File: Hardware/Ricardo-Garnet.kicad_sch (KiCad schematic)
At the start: 46 parts, among them J1 RBUS, P4 IN+, P5 IN-, P6 MOTOR1, P7 MOTOR2, P9 MOTOR3, U1 ESP32-S3, Y2 R940000171

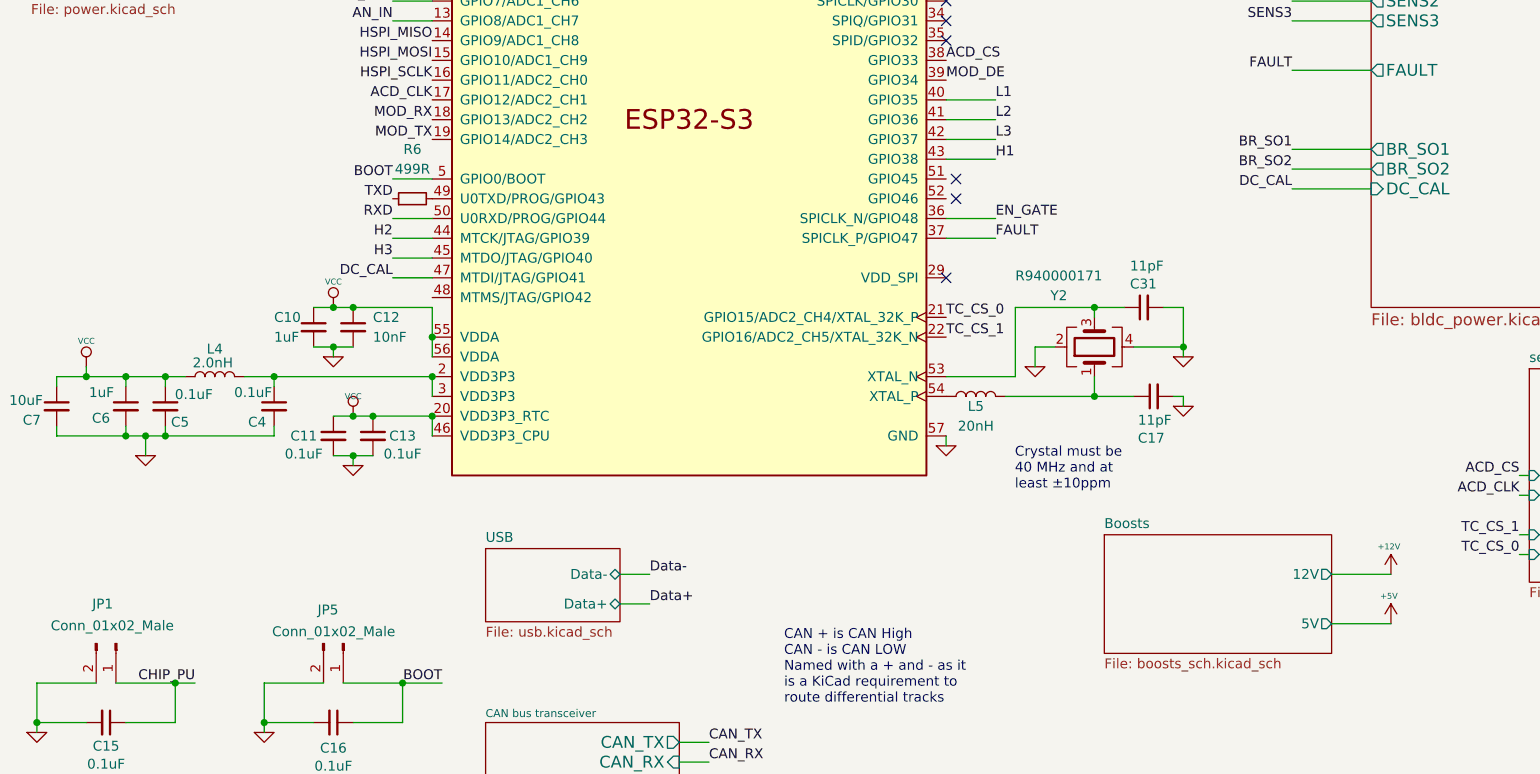
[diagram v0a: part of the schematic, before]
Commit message: removed voltage pt sensing capabilities
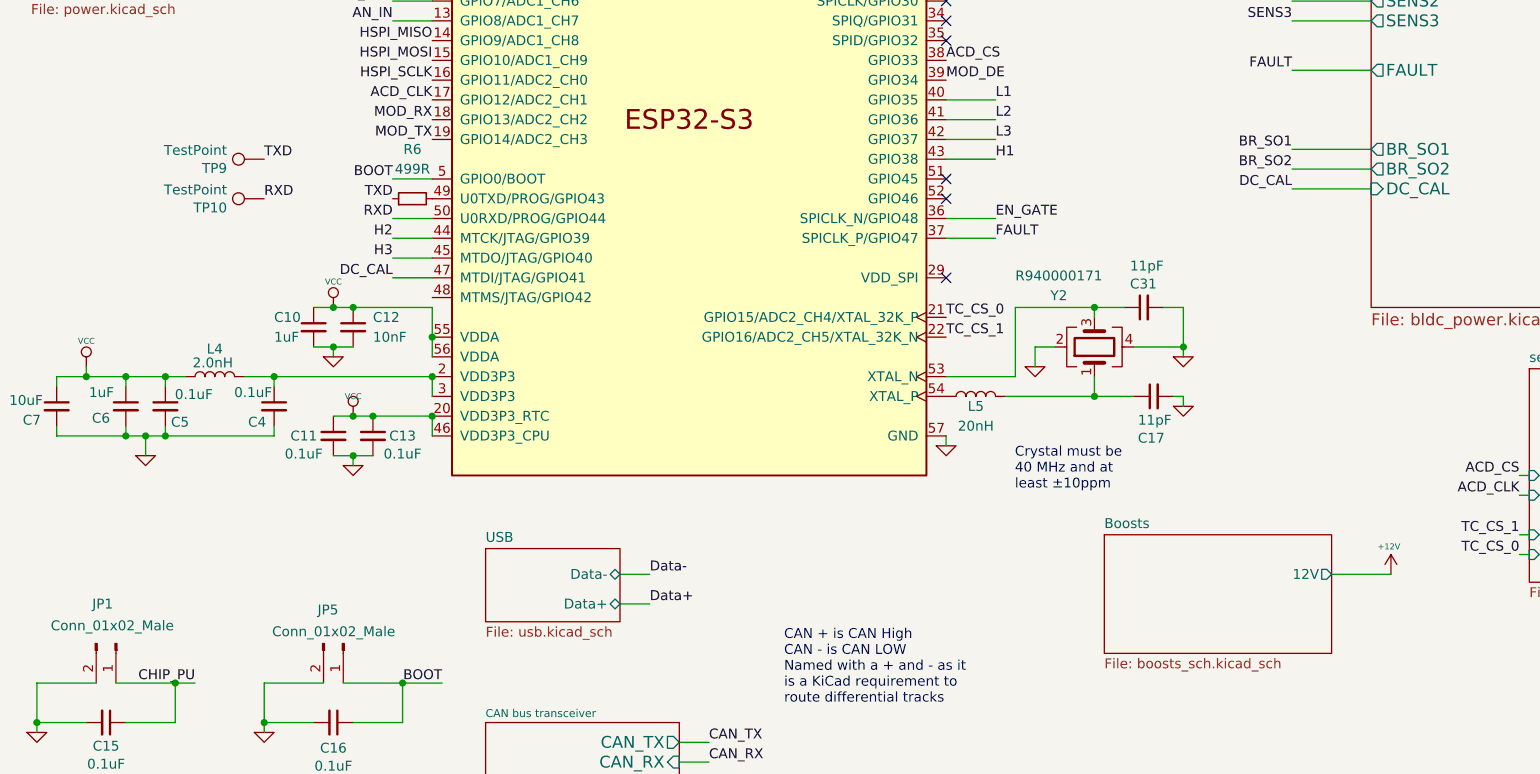
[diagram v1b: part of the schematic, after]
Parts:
- added TP10, TP9: TestPoint, TestPoint:TestPoint_Pad_D1.0mm, symbol Connector:TestPoint
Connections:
- net RXD: now also TP10.1
- net TXD: now also TP9.1
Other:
- sheet Boosts ports: added none; removed 5V
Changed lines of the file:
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@@
 	)
 	(no_connect
-		(at 134.62 104.14)
+		(at 133.35 104.14)
 	)
 	(no_connect
-		(at 134.62 101.6)
+		(at 133.35 101.6)
 	)
 	(no_connect
@@
 	(wire
 		(pts
-			(xy 182.88 158.75) (xy 190.5 158.75)
-		)
-		(stroke
-			(width 0)
-			(type default)
-		)
-	)
-	(wire
-		(pts
 			(xy 220.98 26.67) (xy 220.98 29.21)
 		)
@@
 		)
 	)
+	(label "RXD"
+		(at 45.72 104.14 0)
+		(effects
+			(font
+				(size 1.27 1.27)
+			)
+			(justify left bottom)
+		)
+	)
 	(label "CAN-"
 		(at 102.87 182.88 0)
@@
 		)
 	)
+	(label "TXD"
+		(at 45.72 99.06 0)
+		(effects
+			(font
+				(size 1.27 1.27)
+			)
+			(justify left bottom)
+		)
+	)
 	(label "AN_IN"
 		(at 238.76 21.59 0)
@@
 	)
 	(symbol
+		(lib_id "Connector:TestPoint")
+		(at 45.72 99.06 90)
+		(unit 1)
+		(exclude_from_sim no)
+		(in_bom yes)
+		(on_board yes)
+		(dnp no)
+		(property "Reference" "TP9"
+			(at 40.9448 100.2284 90)
+			(effects
+				(font
+					(size 1.27 1.27)
+				)
+				(justify left)
+			)
+		)
+		(property "Value" "TestPoint"
+			(at 40.9448 97.917 90)
+			(effects
+				(font
+					(size 1.27 1.27)
+				)
+				(justify left)
+			)
+		)
+		(property "Footprint" "TestPoint:TestPoint_Pad_D1.0mm"
+			(at 45.72 93.98 0)
+			(effects
+				(font
+					(size 1.27 1.27)
+				)
+				(hide yes)
+			)
+		)
+		(property "Datasheet" "~"
+			(at 45.72 93.98 0)
+			(effects
+				(font
+					(size 1.27 1.27)
+				)
+				(hide yes)
+			)
+		)
+		(property "Description" ""
+			(at 45.72 99.06 0)
+			(effects
+				(font
+					(size 1.27 1.27)
+				)
+				(hide yes)
+			)
+		)
+		(pin "1"
+		)
+		(instances
+			(project "Ricardo-Garnet"
+				(path "/a4c716a5-e5f4-4cd7-812e-2c21e63f692f"
+					(reference "TP9")
+					(unit 1)
+				)
+			)
+		)
+	)
+	(symbol
 		(lib_id "Device:LED_Small")
 		(at 25.4 38.1 0)
@@
 	)
 	(symbol
-		(lib_name "+5V_9")
-		(lib_id "BLDC_4-rescue:+5V")
-		(at 190.5 158.75 0)
-		(unit 1)
-		(exclude_from_sim no)
-		(in_bom yes)
-		(on_board yes)
-		(dnp no)
-		(property "Reference" "#PWR065"
-			(at 190.5 156.464 0)
-			(effects
-				(font
-					(size 0.508 0.508)
-				)
-				(hide yes)
-			)
-		)
-		(property "Value" "+5V"
-			(at 190.246 155.194 0)
-			(effects
-				(font
-					(size 0.762 0.762)
-				)
-			)
-		)
-		(property "Footprint" ""
-			(at 190.5 158.75 0)
-			(effects
-				(font
-					(size 1.524 1.524)
-				)
-				(hide yes)
-			)
-		)
-		(property "Datasheet" ""
-			(at 190.5 158.75 0)
-			(effects
-				(font
-					(size 1.524 1.524)
-				)
-				(hide yes)
-			)
-		)
-		(property "Description" ""
-			(at 190.5 158.75 0)
-			(effects
-				(font
-					(size 1.27 1.27)
-				)
-			)
-		)
-		(pin "1"
-		)
-		(instances
-			(project "BLDC_4"
-				(path "/a4c716a5-e5f4-4cd7-812e-2c21e63f692f"
-					(reference "#PWR065")
-					(unit 1)
-				)
-			)
-		)
-	)
-	(symbol
 		(lib_name "GND-RESCUE-BLDC_4_20")
 		(lib_id "BLDC_4-rescue:GND-RESCUE-BLDC_4")
@@
 	)
 	(symbol
+		(lib_id "Connector:TestPoint")
+		(at 45.72 104.14 90)
+		(unit 1)
+		(exclude_from_sim no)
+		(in_bom yes)
+		(on_board yes)
+		(dnp no)
+		(property "Reference" "TP10"
+			(at 40.9448 105.3084 90)
+			(effects
+				(font
+					(size 1.27 1.27)
+				)
+				(justify left)
+			)
+		)
+		(property "Value" "TestPoint"
+			(at 40.9448 102.997 90)
+			(effects
+				(font
+					(size 1.27 1.27)
+				)
+				(justify left)
+			)
+		)
+		(property "Footprint" "TestPoint:TestPoint_Pad_D1.0mm"
+			(at 45.72 99.06 0)
+			(effects
+				(font
+					(size 1.27 1.27)
+				)
+				(hide yes)
+			)
+		)
+		(property "Datasheet" "~"
+			(at 45.72 99.06 0)
+			(effects
+				(font
+					(size 1.27 1.27)
+				)
+				(hide yes)
+			)
+		)
+		(property "Description" ""
+			(at 45.72 104.14 0)
+			(effects
+				(font
+					(size 1.27 1.27)
+				)
+				(hide yes)
+			)
+		)
+		(pin "1"
+		)
+		(instances
+			(project "Ricardo-Garnet"
+				(path "/a4c716a5-e5f4-4cd7-812e-2c21e63f692f"
+					(reference "TP10")
+					(unit 1)
+				)
+			)
+		)
+	)
+	(symbol
 		(lib_id "Device:C_Small")
 		(at 46.99 130.81 0)
@@
 		)
 		(instances
-			(project "BLDC_4"
+			(project "Ricardo-Garnet"
 				(path "/a4c716a5-e5f4-4cd7-812e-2c21e63f692f"
 					(page "6")
@@
 		)
 		(instances
-			(project "BLDC_4"
+			(project "Ricardo-Garnet"
 				(path "/a4c716a5-e5f4-4cd7-812e-2c21e63f692f"
 					(page "7")
@@
 		)
 		(instances
-			(project "BLDC_4"
+			(project "Ricardo-Garnet"
 				(path "/a4c716a5-e5f4-4cd7-812e-2c21e63f692f"
 					(page "2")
@@
 		)
 		(instances
-			(project "BLDC_4"
+			(project "Ricardo-Garnet"
 				(path "/a4c716a5-e5f4-4cd7-812e-2c21e63f692f"
 					(page "5")
@@
 		)
 		(instances
-			(project "BLDC_4"
+			(project "Ricardo-Garnet"
 				(path "/a4c716a5-e5f4-4cd7-812e-2c21e63f692f"
 					(page "3")
@@
 			)
 		)
-		(pin "5V" output
-			(at 182.88 158.75 0)
-			(effects
-				(font
-					(size 1.27 1.27)
-				)
-				(justify right)
-			)
-		)
 		(instances
-			(project "BLDC_4"
+			(project "Ricardo-Garnet"
 				(path "/a4c716a5-e5f4-4cd7-812e-2c21e63f692f"
 					(page "4")
@@
 		)
 		(instances
-			(project "BLDC_4"
+			(project "Ricardo-Garnet"
 				(path "/a4c716a5-e5f4-4cd7-812e-2c21e63f692f"
 					(page "8")

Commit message: chatting to fang
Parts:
- C2, C41: footprint CRF1:SMD-0603_c -> Capacitor_SMD:C_0603_1608Metric
- R1, R3: footprint CRF1:SMD-0603_r -> Resistor_SMD:R_0603_1608Metric
- R2, R4: footprint CRF1:SMD-0603_r -> Resistor_SMD:R_0402_1005Metric
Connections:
- net ACD_CS: now also U1.36 (SPICLK_N/GPIO48); no longer U1.38 (GPIO33)
- net AN_IN: now also U1.12 (GPIO7/ADC1_CH6); no longer U1.13 (GPIO8/ADC1_CH7)
- net BR_SO2: now also U1.10 (GPIO5/ADC1_CH4); no longer U1.12 (GPIO7/ADC1_CH6)
- net EN_GATE: now also U1.39 (GPIO34); no longer U1.36 (SPICLK_N/GPIO48)
- net FAULT: now also U1.48 (MTMS/JTAG/GPIO42); no longer U1.37 (SPICLK_P/GPIO47)
- net H1: now also U1.45 (MTDO/JTAG/GPIO40); no longer U1.43 (GPIO38)
- net H2: now also U1.43 (GPIO38); no longer U1.44 (MTCK/JTAG/GPIO39)
- net H3: now also U1.41 (GPIO36); no longer U1.45 (MTDO/JTAG/GPIO40)
- net L1: now also U1.44 (MTCK/JTAG/GPIO39); no longer U1.40 (GPIO35)
- net L2: now also U1.42 (GPIO37); no longer U1.41 (GPIO36)
- net L3: now also U1.40 (GPIO35); no longer U1.42 (GPIO37)
- net MOD_DE: now also U1.27 (GPIO21); no longer U1.39 (GPIO34)
- net MOS_TEMP: now also U1.13 (GPIO8/ADC1_CH7); no longer U1.10 (GPIO5/ADC1_CH4)
- net SENS1: now also U1.7 (GPIO2/ADC1_CH1); no longer U1.6 (GPIO1/ADC1_CH0)
- net SENS2: now also U1.9 (GPIO4/ADC1_CH3); no longer U1.7 (GPIO2/ADC1_CH1)
- net SENS3: now also U1.6 (GPIO1/ADC1_CH0); no longer U1.9 (GPIO4/ADC1_CH3)
- no-connect marks 12 -> 15

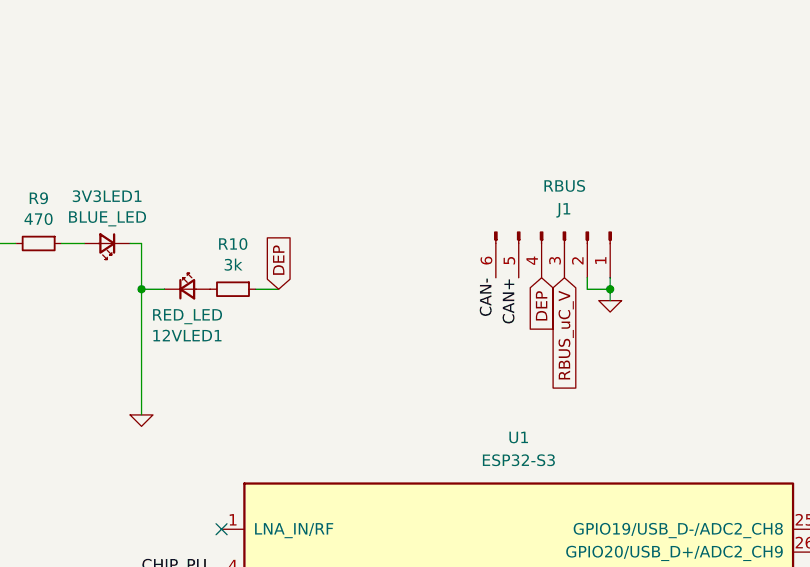
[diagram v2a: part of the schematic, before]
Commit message: updated settled pcb design
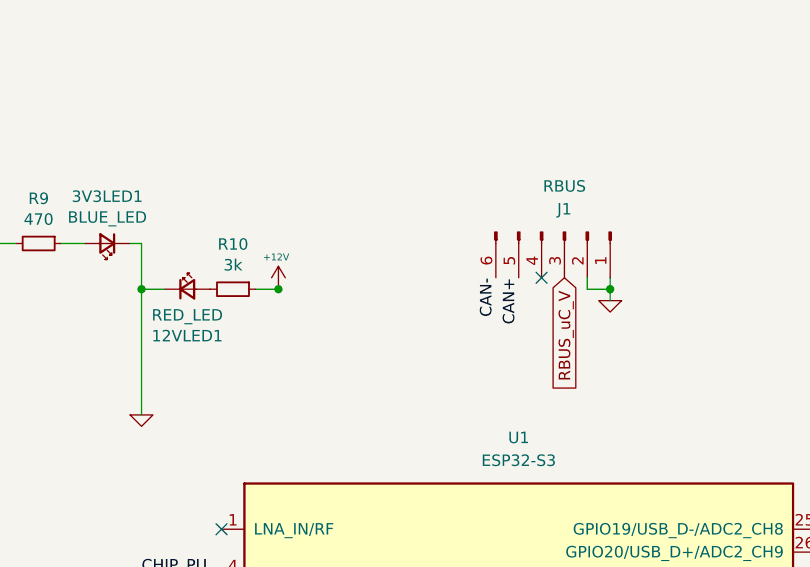
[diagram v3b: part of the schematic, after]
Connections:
- net +12V: now also R10.1
- net DEP: no longer names the net of J1.4 (Pin_4)
- net DEP: no longer R10.1
- no-connect marks 15 -> 16
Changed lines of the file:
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@@
 	)
 	(junction
+		(at 73.6308 26.67)
+		(diameter 0)
+		(color 0 0 0 0)
+	)
+	(junction
 		(at 33.02 127)
 		(diameter 0)
@@
 	)
 	(no_connect
+		(at 102.87 25.4)
+	)
+	(no_connect
 		(at 133.35 109.22)
 	)
@@
 	(wire
 		(pts
-			(xy 73.66 26.67) (xy 71.12 26.67)
+			(xy 73.66 26.67) (xy 73.6308 26.67)
 		)
 		(stroke
@@
 	(wire
 		(pts
+			(xy 73.6308 26.67) (xy 71.12 26.67)
+		)
+		(stroke
+			(width 0)
+			(type default)
+		)
+	)
+	(wire
+		(pts
 			(xy 30.48 184.15) (xy 30.48 186.69)
 		)
@@
 		)
 	)
-	(global_label "DEP"
-		(shape input)
-		(at 73.66 26.67 90)
-		(fields_autoplaced yes)
-		(effects
-			(font
-				(size 1.27 1.27)
-			)
-			(justify left)
-		)
-		(property "Intersheetrefs" "${INTERSHEET_REFS}"
-			(at 73.66 20.65 90)
-			(effects
-				(font
-					(size 1.27 1.27)
-				)
-				(justify left)
-				(hide yes)
-			)
-		)
-	)
-	(global_label "DEP"
-		(shape input)
-		(at 102.87 25.4 270)
-		(fields_autoplaced yes)
-		(effects
-			(font
-				(size 1.27 1.27)
-			)
-			(justify right)
-		)
-		(property "Intersheetrefs" "${INTERSHEET_REFS}"
-			(at 102.87 31.42 90)
-			(effects
-				(font
-					(size 1.27 1.27)
-				)
-				(justify right)
-				(hide yes)
-			)
-		)
-	)
 	(global_label "V_SUPPLY"
 		(shape input)
@@
 					(unit 1)
 				)
+			)
+		)
+	)
+	(symbol
+		(lib_name "+5V_9")
+		(lib_id "BLDC_4-rescue:+5V")
+		(at 73.6308 26.67 0)
+		(unit 1)
+		(exclude_from_sim no)
+		(in_bom yes)
+		(on_board yes)
+		(dnp no)
+		(property "Reference" "#PWR052"
+			(at 73.6308 24.384 0)
+			(effects
+				(font
+					(size 0.508 0.508)
+				)
+				(hide yes)
+			)
+		)
+		(property "Value" "+12V"
+			(at 73.3768 23.114 0)
+			(effects
+				(font
+					(size 0.762 0.762)
+				)
+			)
+		)
+		(property "Footprint" ""
+			(at 73.6308 26.67 0)
+			(effects
+				(font
+					(size 1.524 1.524)
+				)
+				(hide yes)
+			)
+		)
+		(property "Datasheet" ""
+			(at 73.6308 26.67 0)
+			(effects
+				(font
+					(size 1.524 1.524)
+				)
+				(hide yes)
+			)
+		)
+		(property "Description" ""
+			(at 73.6308 26.67 0)
+			(effects
+				(font
+					(size 1.27 1.27)
+				)
+			)
+		)
+		(pin "1"
+		)
+		(instances
+			(project "Ricardo-Garnet"
+				(path "/a4c716a5-e5f4-4cd7-812e-2c21e63f692f"
+					(reference "#PWR052")
+					(unit 1)
+				)

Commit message: close to 1st done
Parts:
- removed P6: MOTOR1, CRF1:1PAD_4x5mm, symbol BLDC_4-rescue:CONN_1
- removed P7: MOTOR2, CRF1:1PAD_4x5mm, symbol BLDC_4-rescue:CONN_1
- removed P9: MOTOR3, CRF1:1PAD_4x5mm, symbol BLDC_4-rescue:CONN_1
- removed R53, R54: SHUNT, CRF1:WSLP2726, symbol crf_1:SHUNT
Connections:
- net ACD_CLK: now also U1.12 (GPIO7/ADC1_CH6); no longer U1.17 (GPIO12/ADC2_CH1)
- net ACD_CS: now also U1.21 (GPIO15/ADC2_CH4/XTAL_32K_P); no longer U1.36 (SPICLK_N/GPIO48)
- net AN_IN: now also U1.18 (GPIO13/ADC2_CH2); no longer U1.12 (GPIO7/ADC1_CH6)
- net BR_SO1: now also U1.6 (GPIO1/ADC1_CH0); no longer U1.11 (GPIO6/ADC1_CH5)
- net BR_SO2: now also U1.7 (GPIO2/ADC1_CH1); no longer U1.10 (GPIO5/ADC1_CH4)
- net HSPI_MISO: now also U1.15 (GPIO10/ADC1_CH9); no longer U1.14 (GPIO9/ADC1_CH8)
- net HSPI_MOSI: now also U1.16 (GPIO11/ADC2_CH0); no longer U1.15 (GPIO10/ADC1_CH9)
- net HSPI_SCLK: now also U1.17 (GPIO12/ADC2_CH1); no longer U1.16 (GPIO11/ADC2_CH0)
- net MOD_DE: now also U1.36 (SPICLK_N/GPIO48); no longer U1.27 (GPIO21)
- net MOD_RX: now also U1.14 (GPIO9/ADC1_CH8); no longer U1.18 (GPIO13/ADC2_CH2)
- net MOD_TX: now also U1.13 (GPIO8/ADC1_CH7); no longer U1.19 (GPIO14/ADC2_CH3)
- net MOS_TEMP: now also U1.19 (GPIO14/ADC2_CH3); no longer U1.13 (GPIO8/ADC1_CH7)
- net SENS1: now also U1.10 (GPIO5/ADC1_CH4); no longer U1.7 (GPIO2/ADC1_CH1)
- net SENS2: now also U1.11 (GPIO6/ADC1_CH5); no longer U1.9 (GPIO4/ADC1_CH3)
- net SENS3: now also U1.9 (GPIO4/ADC1_CH3); no longer U1.6 (GPIO1/ADC1_CH0)
- net TC_CS_0: now also U1.22 (GPIO16/ADC2_CH5/XTAL_32K_N); no longer U1.21 (GPIO15/ADC2_CH4/XTAL_32K_P)
- net TC_CS_1: now also U1.27 (GPIO21); no longer U1.22 (GPIO16/ADC2_CH5/XTAL_32K_N)
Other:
- sheet Mosfet driver ports: added GH_A, GH_B, GH_C, GL_A, GL_B, GL_C, SH_A, SH_B, SH_C, SL_A, SL_B, SL_C, SN1, SN2, SP1, SP2; removed H1_LOW, H1_VS, H2_LOW, H2_VS, H3_LOW, H3_VS, M_H1, M_H2, M_H3, M_L1, M_L2, M_L3, SH1_A, SH1_B, SH2_A, SH2_B
- sheet Power MOSFETS ports: added GH_A, GH_B, GH_C, GL_A, GL_B, GL_C, SH_A, SH_B, SH_C, SL_A, SL_B, SL_C, SN1, SN2, SP1, SP2; removed H1_LOW, H1_VS, H2_LOW, H2_VS, H3_LOW, H3_VS, M_H1, M_H2, M_H3, M_L1, M_L2, M_L3, PHASE_1, PHASE_2, PHASE_3

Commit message: final touches and adding encoder
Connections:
- net ENCODER_CS: now reaches U1.37 (SPICLK_P/GPIO47)
- no-connect marks 16 -> 15
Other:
- sheet sensors ports: added ENCODER_CS; removed none
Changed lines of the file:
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@@
 	)
 	(no_connect
-		(at 133.35 109.22)
-	)
-	(no_connect
 		(at 133.35 86.36)
 	)
@@
 	(wire
 		(pts
+			(xy 133.35 109.22) (xy 139.7 109.22)
+		)
+		(stroke
+			(width 0)
+			(type default)
+		)
+	)
+	(wire
+		(pts
 			(xy 182.88 152.4) (xy 190.5 152.4)
 		)
@@
 	(wire
 		(pts
+			(xy 207.01 129.54) (xy 208.28 129.54)
+		)
+		(stroke
+			(width 0)
+			(type default)
+		)
+	)
+	(wire
+		(pts
 			(xy 57.15 118.11) (xy 67.31 118.11)
 		)
@@
 		)
 	)
+	(label "ENCODER_CS"
+		(at 207.01 129.54 180)
+		(effects
+			(font
+				(size 1.27 1.27)
+			)
+			(justify right bottom)
+		)
+	)
 	(label "RXD"
 		(at 62.23 106.68 180)
@@
 		)
 	)
+	(label "ENCODER_CS"
+		(at 139.7 109.22 0)
+		(effects
+			(font
+				(size 1.27 1.27)
+			)
+			(justify left bottom)
+		)
+	)
 	(label "HSPI_SCLK"
 		(at 62.23 91.44 180)
@@
 			)
 		)
+		(pin "ENCODER_CS" input
+			(at 208.28 129.54 180)
+			(effects
+				(font
+					(size 1.27 1.27)
+				)
+				(justify left)
+			)
+		)

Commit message: mounting holes looking rough
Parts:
- added H1, H2, H3, H4: MountingHole_Pad, MountingHole:MountingHole_3.2mm_M3_DIN965_Pad, symbol Mechanical:MountingHole_Pad
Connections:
- net GND: now also H1.1, H2.1, H3.1, H4.1
